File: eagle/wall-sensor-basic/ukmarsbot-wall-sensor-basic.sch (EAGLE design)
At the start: 22 parts, among them Q1 2N2222*, T1 BPW96B, T2 BPW96B, T3 BPW96B

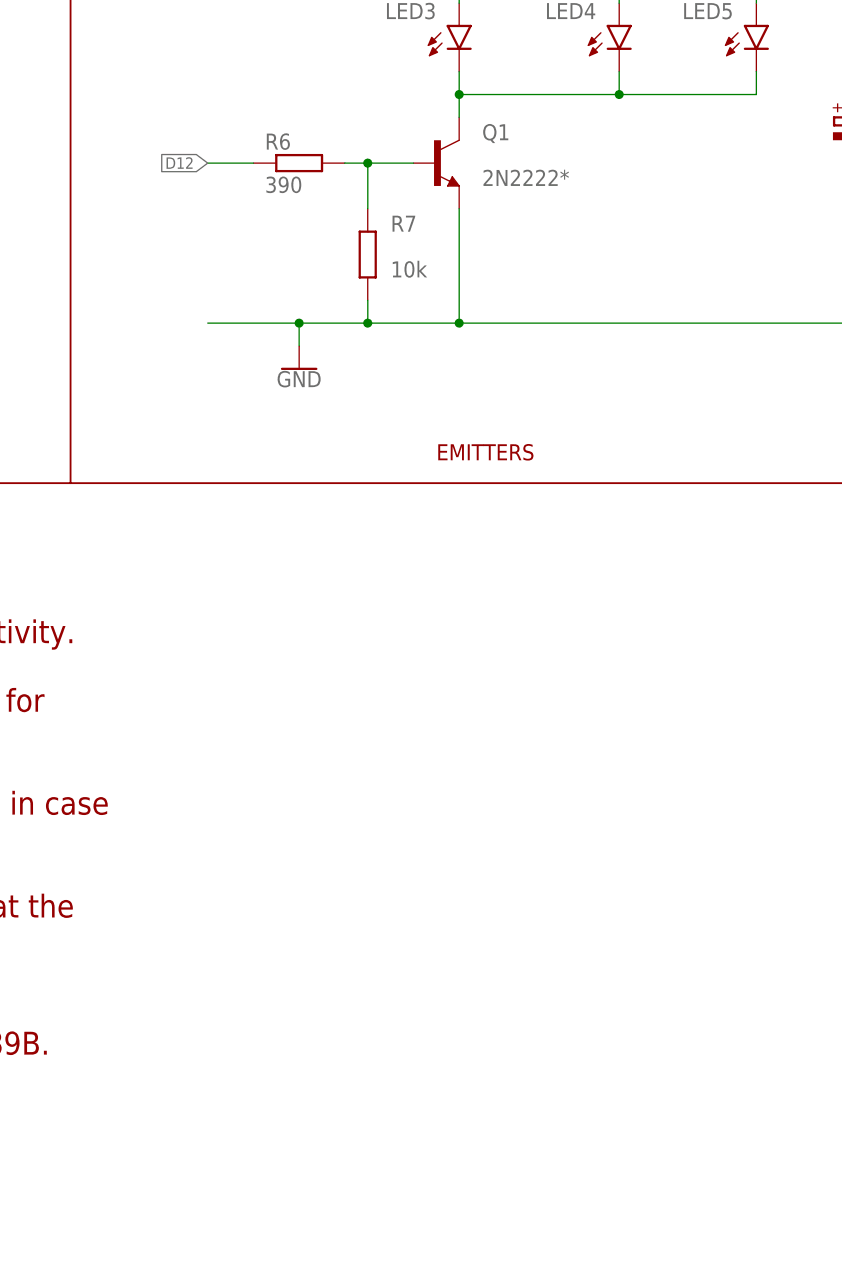
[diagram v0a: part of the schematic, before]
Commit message: Update Basic Wall Sensor board and library with larger pads/holes
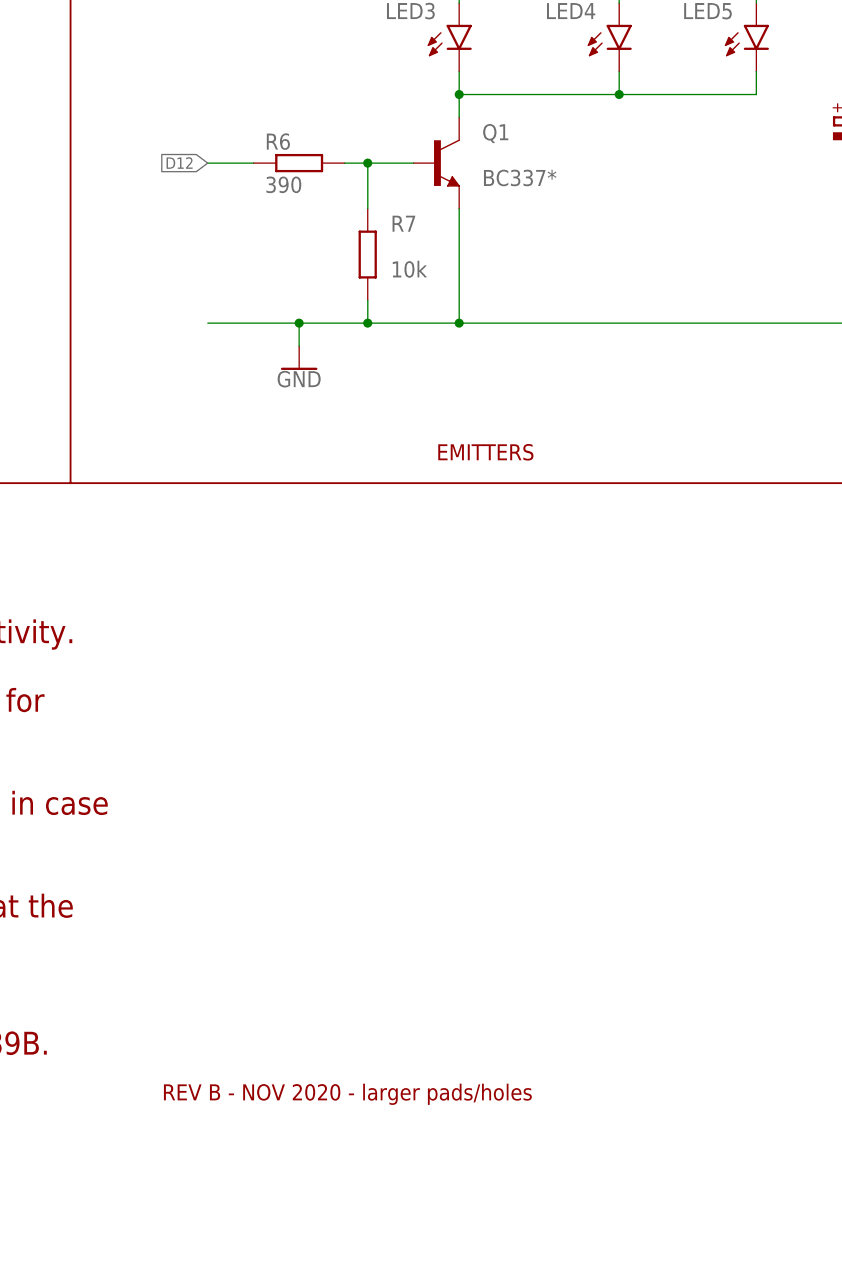
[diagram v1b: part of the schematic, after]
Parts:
- Q1: value 2N2222* -> BC337*
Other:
- note added: "REV B - NOV 2020 - larger pads/holes"
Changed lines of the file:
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@@
 <parts>
 <part name="J1" library="ukmarsbot" deviceset="CONN_14" device=""/>
-<part name="FRAME1" library="ukmarsbot" deviceset="FRAME-A4L" device=""/>
+<part name="FRAME1" library="ukmarsbot" deviceset="FRAME-A4L" device="">
+<attribute name="REV" value="1.0"/>
+</part>
 <part name="LED3" library="ukmarsbot" deviceset="LED" device="-SIDE" value="SFH4550"/>
 <part name="LED4" library="ukmarsbot" deviceset="LED" device="-SIDE" value="SFH4550"/>
@@
 <attribute name="VOLTAGE" value="16V"/>
 </part>
-<part name="Q1" library="ukmarsbot" deviceset="TRANS_NPN" device="" value="2N2222*"/>
+<part name="Q1" library="ukmarsbot" deviceset="TRANS_NPN" device="" value="BC337*"/>
 <part name="SUPPLY1" library="ukmarsbot" deviceset="5V" device=""/>
 <part name="SUPPLY2" library="ukmarsbot" deviceset="5V" device=""/>
@@
 Possible alternatives include BC337-16, ZTX451, ZTX651, ZTX689B.
 </text>
+<text x="180.34" y="22.86" size="1.778" layer="94">REV B - NOV 2020 - larger pads/holes</text>
 </plain>
 <instances>
@@
 <attribute name="NAME" x="17.78" y="157.988" size="1.778" layer="95" font="vector"/>
 </instance>
-<instance part="FRAME1" gate="G$1" x="0" y="0"/>
+<instance part="FRAME1" gate="G$1" x="0" y="0" smashed="yes">
+<attribute name="DRAWING_NAME" x="181.61" y="11.43" size="2.54" layer="94" font="vector"/>
+<attribute name="LAST_DATE_TIME" x="181.61" y="6.35" size="2.286" layer="94" font="vector"/>
+<attribute name="SHEET" x="195.58" y="1.27" size="2.54" layer="94" font="vector"/>
+<attribute name="DESIGNER" x="226.26" y="6.35" size="2.54" layer="94" font="vector"/>
+<attribute name="REV" x="234.92" y="1.17" size="2.54" layer="94" font="vector"/>
+</instance>
 <instance part="LED3" gate="D1" x="213.36" y="142.24" smashed="yes">
 <attribute name="NAME" x="210.82" y="144.78" size="1.778" layer="95" font="vector" rot="R180"/>

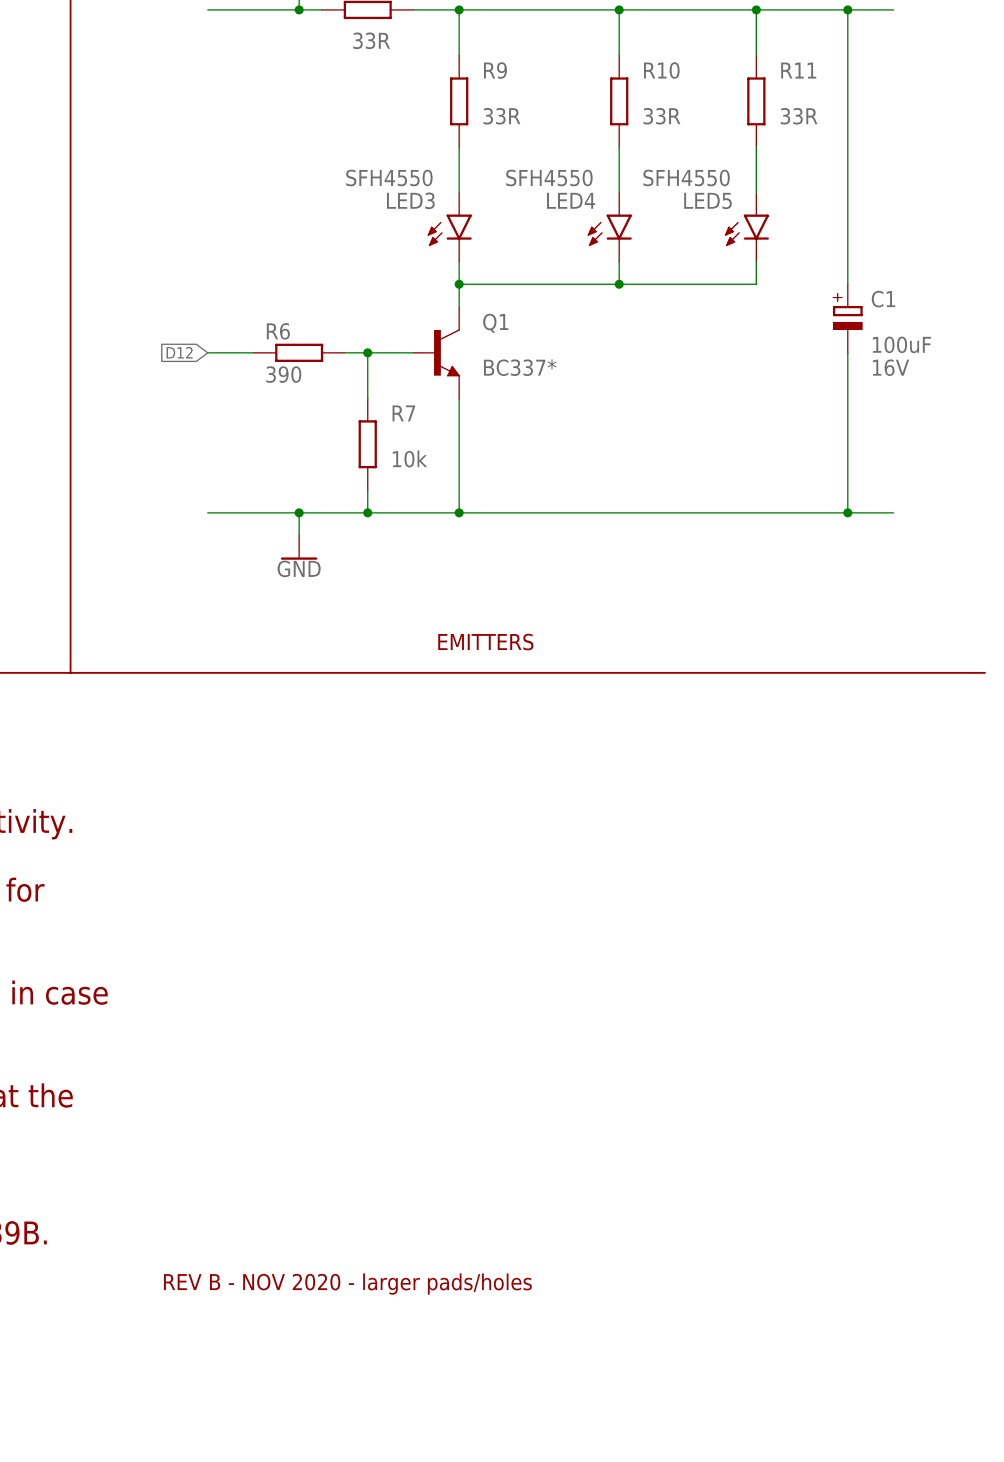
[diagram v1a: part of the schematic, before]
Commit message: Remove deprecated SFH4550 references
Board 20190815C has generic emitters in schematic and on the silk screen.
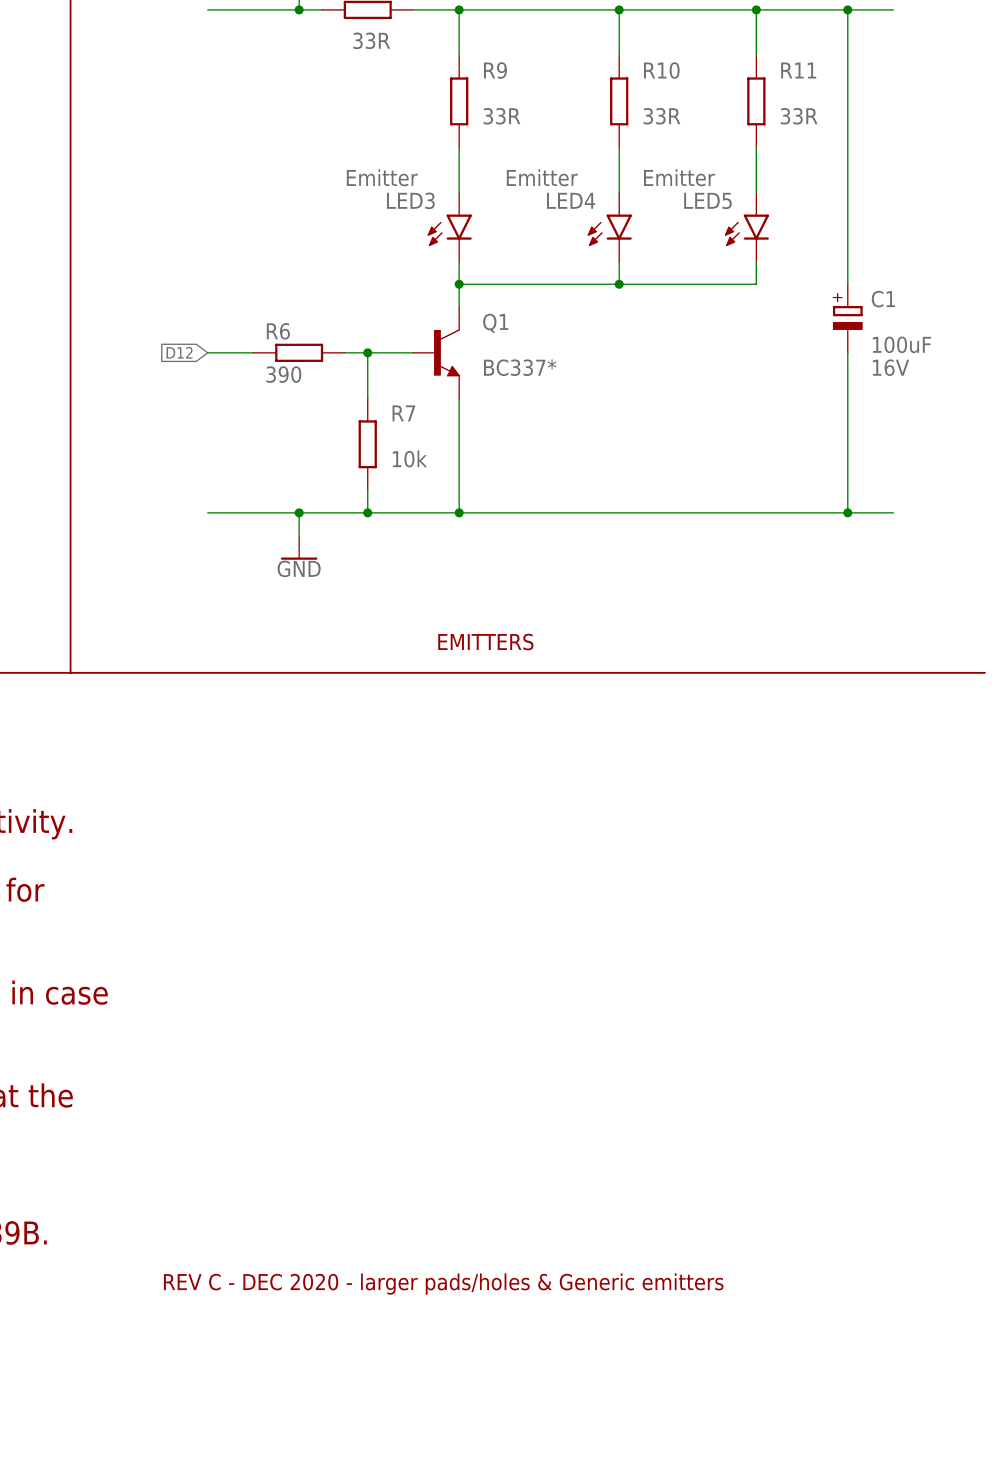
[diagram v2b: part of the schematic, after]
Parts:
- LED3, LED4, LED5: value SFH4550 -> Emitter
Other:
- note added: "REV C - DEC 2020 - larger pads/holes & Generic emitters"
- note removed: "REV B - NOV 2020 - larger pads/holes"
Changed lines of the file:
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@@
 <?xml version="1.0" encoding="utf-8"?>
 <!DOCTYPE eagle SYSTEM "eagle.dtd">
-<eagle version="7.6.0">
+<eagle version="7.5.0">
 <drawing>
 <settings>
@@
 <attribute name="REV" value="1.0"/>
 </part>
-<part name="LED3" library="ukmarsbot" deviceset="LED" device="-SIDE" value="SFH4550"/>
-<part name="LED4" library="ukmarsbot" deviceset="LED" device="-SIDE" value="SFH4550"/>
-<part name="LED5" library="ukmarsbot" deviceset="LED" device="-SIDE" value="SFH4550"/>
+<part name="LED3" library="ukmarsbot" deviceset="LED" device="-SIDE" value="Emitter"/>
+<part name="LED4" library="ukmarsbot" deviceset="LED" device="-SIDE" value="Emitter"/>
+<part name="LED5" library="ukmarsbot" deviceset="LED" device="-SIDE" value="Emitter"/>
 <part name="T1" library="ukmarsbot" deviceset="PHOTOTRANSISTOR" device="SIDE" value="BPW96B">
 <attribute name="POS" value="Left"/>
@@
 Possible alternatives include BC337-16, ZTX451, ZTX651, ZTX689B.
 </text>
-<text x="180.34" y="22.86" size="1.778" layer="94">REV B - NOV 2020 - larger pads/holes</text>
+<text x="180.34" y="22.86" size="1.778" layer="94">REV C - DEC 2020 - larger pads/holes &amp; Generic emitters</text>
 </plain>
 <instances>
